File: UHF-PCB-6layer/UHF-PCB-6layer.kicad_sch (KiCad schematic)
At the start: 1 part, among them U1 XC7A100T-CSG324

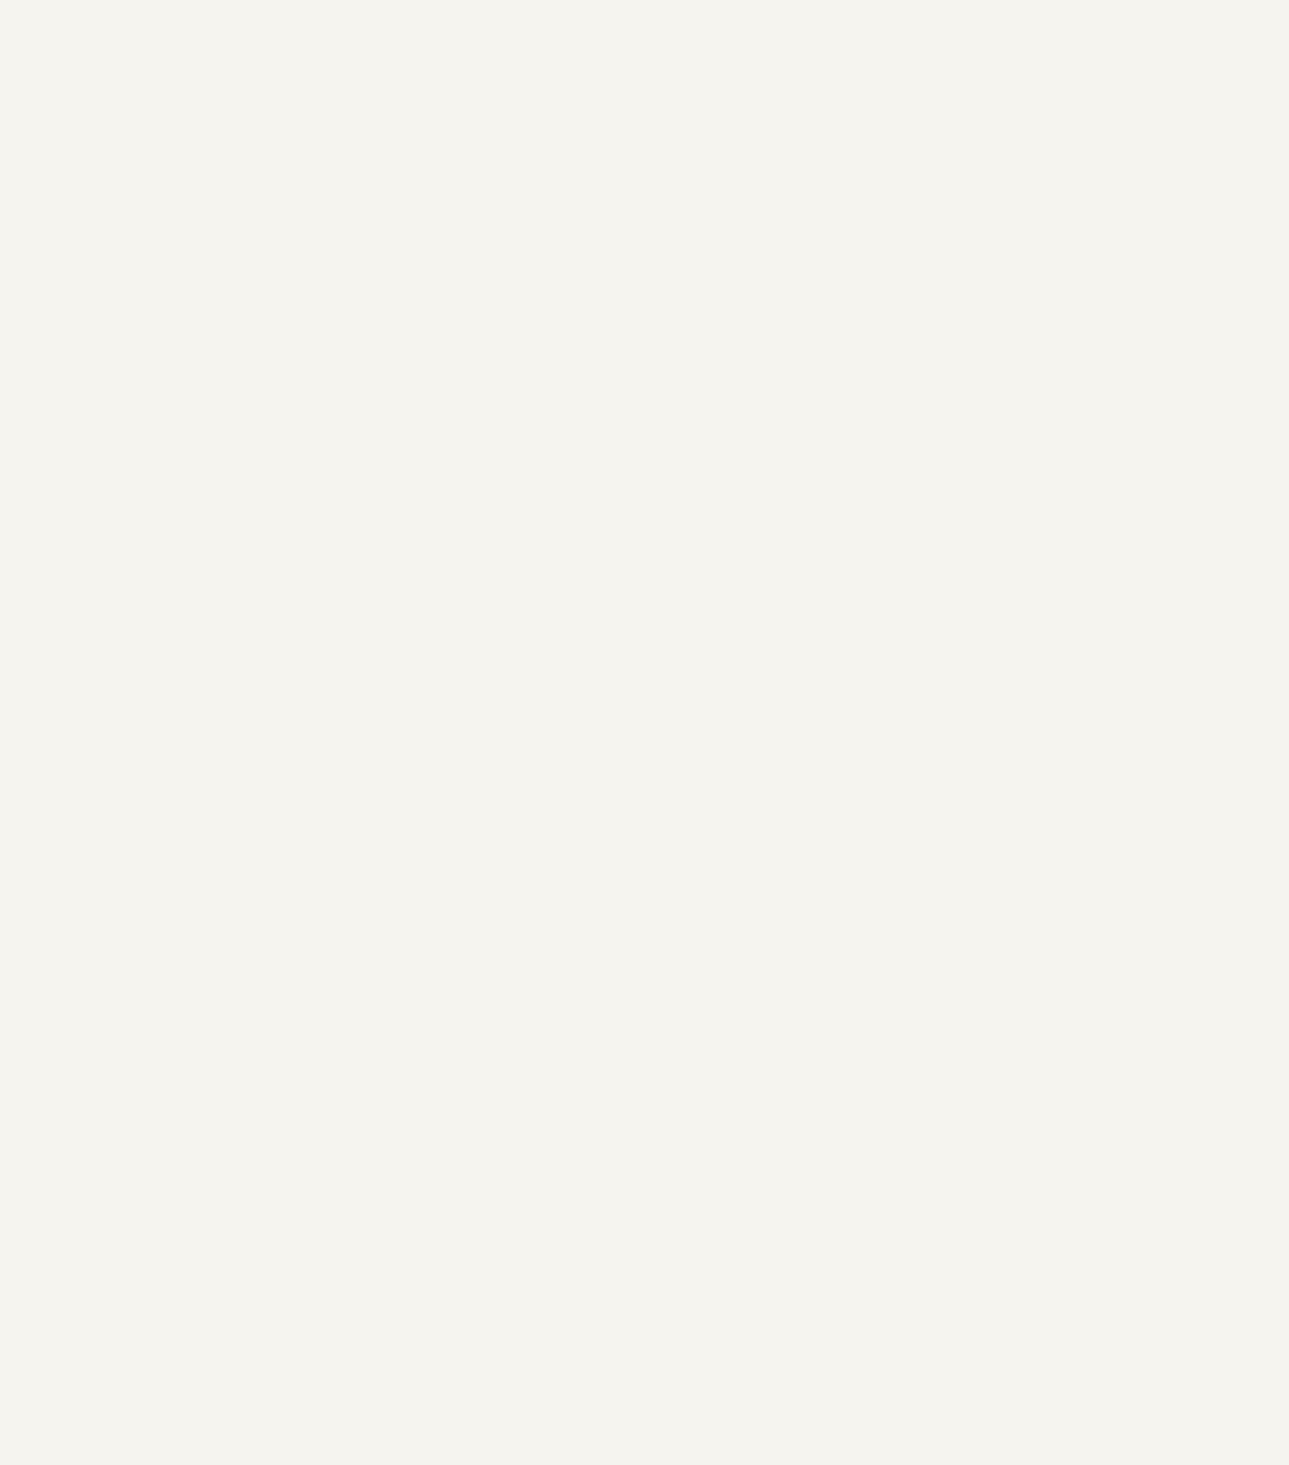
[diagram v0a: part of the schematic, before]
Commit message: added to pcb design, added all comps but mixer and microcontroller
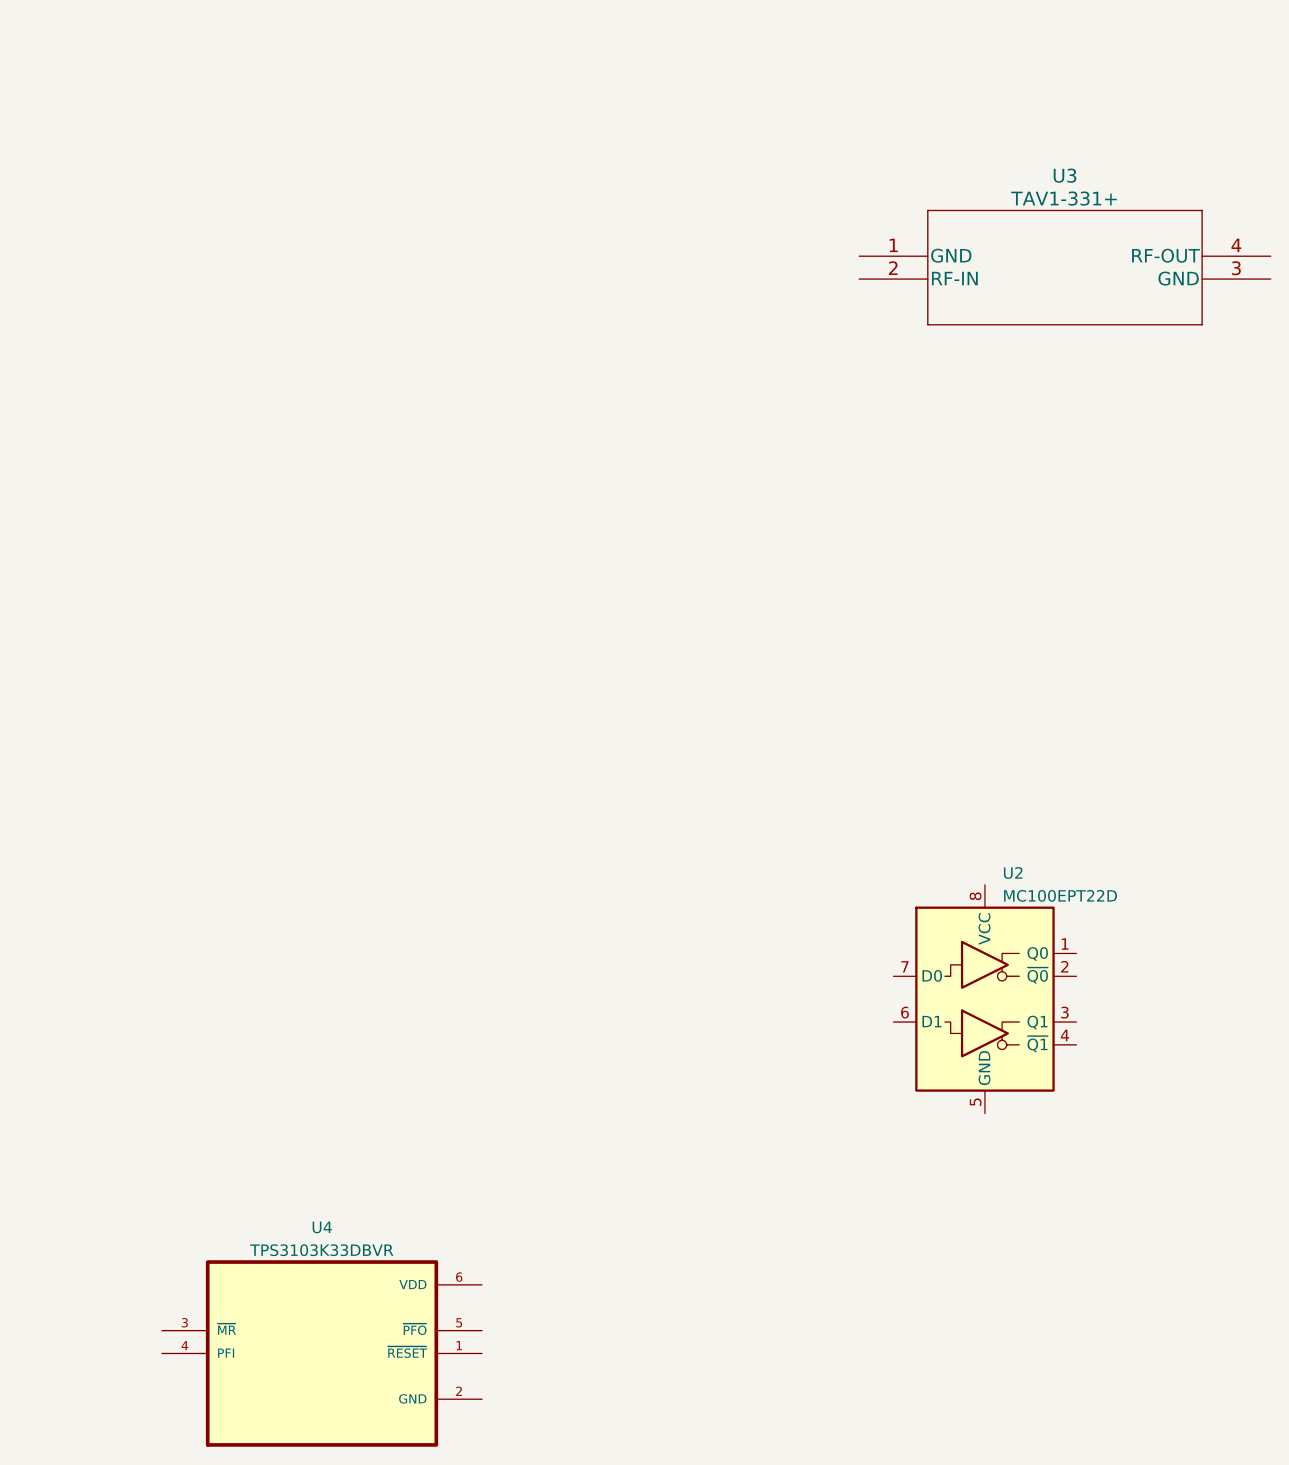
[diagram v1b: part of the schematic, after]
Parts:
- added U2: MC100EPT22D, Package_SO:SOIC-8_3.9x4.9mm_P1.27mm, symbol Interface:MC100EPT22D
- added U3: TAV1-331+, TE2769_MNC, symbol 2023-12-16_21-42-08:TAV1-331+
- added U4: TPS3103K33DBVR, SOT95P280X145-6N, symbol TPS3103K33DBVR:TPS3103K33DBVR
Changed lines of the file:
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@@
+    )
+  )
+  (symbol (lib_id "2023-12-16_21-42-08:TAV1-331+") (at 378.46 52.07 0) (unit 1)
+    (in_bom yes) (on_board yes) (dnp no) (fields_autoplaced)
+    (property "Reference" "U3" (at 401.32 43.18 0)
+      (effects (font (size 1.524 1.524)))
+    )
+    (property "Value" "TAV1-331+" (at 401.32 45.72 0)
+      (effects (font (size 1.524 1.524)))
+    )
+    (property "Footprint" "TE2769_MNC" (at 401.32 45.974 0)
+      (effects (font (size 1.524 1.524)) hide)
+    )
+    (property "Datasheet" "" (at 378.46 52.07 0)
+      (effects (font (size 1.524 1.524)))
+    )
+    (pin "1")
+    (pin "2")
+    (pin "3")
+    (pin "4")
+    (instances
+      (project "UHF-PCB-6layer"
+        (path "/408f5dbf-8c57-4b84-b0cc-1d788fcf6d08"
+          (reference "U3") (unit 1)
+        )
+      )
+    )
+  )
+  (symbol (lib_id "Interface:MC100EPT22D") (at 392.43 134.62 0) (unit 1)
+    (in_bom yes) (on_board yes) (dnp no) (fields_autoplaced)
+    (property "Reference" "U2" (at 394.3859 120.65 0)
+      (effects (font (size 1.27 1.27)) (justify left))
+    )
+    (property "Value" "MC100EPT22D" (at 394.3859 123.19 0)
+      (effects (font (size 1.27 1.27)) (justify left))
+    )
+    (property "Footprint" "Package_SO:SOIC-8_3.9x4.9mm_P1.27mm" (at 389.89 158.75 0)
+      (effects (font (size 1.27 1.27)) hide)
+    )
+    (property "Datasheet" "https://www.onsemi.com/pub/Collateral/MC100EPT22-D.PDF" (at 393.7 144.78 0)
+      (effects (font (size 1.27 1.27)) hide)
+    )
+    (pin "1")
+    (pin "2")
+    (pin "3")
+    (pin "4")
+    (pin "5")
+    (pin "6")
+    (pin "7")
+    (pin "8")
+    (instances
+      (project "UHF-PCB-6layer"
+        (path "/408f5dbf-8c57-4b84-b0cc-1d788fcf6d08"
+          (reference "U2") (unit 1)
+        )
+      )
+    )
+  )
+  (symbol (lib_id "TPS3103K33DBVR:TPS3103K33DBVR") (at 318.77 173.99 0) (unit 1)
+    (in_bom yes) (on_board yes) (dnp no) (fields_autoplaced)
+    (property "Reference" "U4" (at 318.77 160.02 0)
+      (effects (font (size 1.27 1.27)))
+    )
+    (property "Value" "TPS3103K33DBVR" (at 318.77 162.56 0)
+      (effects (font (size 1.27 1.27)))
+    )
+    (property "Footprint" "SOT95P280X145-6N" (at 318.77 173.99 0)
+      (effects (font (size 1.27 1.27)) (justify left bottom) hide)
+    )
+    (property "Datasheet" "" (at 318.77 173.99 0)
+      (effects (font (size 1.27 1.27)) (justify left bottom) hide)
+    )
+    (pin "1")
+    (pin "2")
+    (pin "3")
+    (pin "4")
+    (pin "5")
+    (pin "6")
+    (instances
+      (project "UHF-PCB-6layer"
+        (path "/408f5dbf-8c57-4b84-b0cc-1d788fcf6d08"
+          (reference "U4") (unit 1)
+        )
+      )
     )
   )

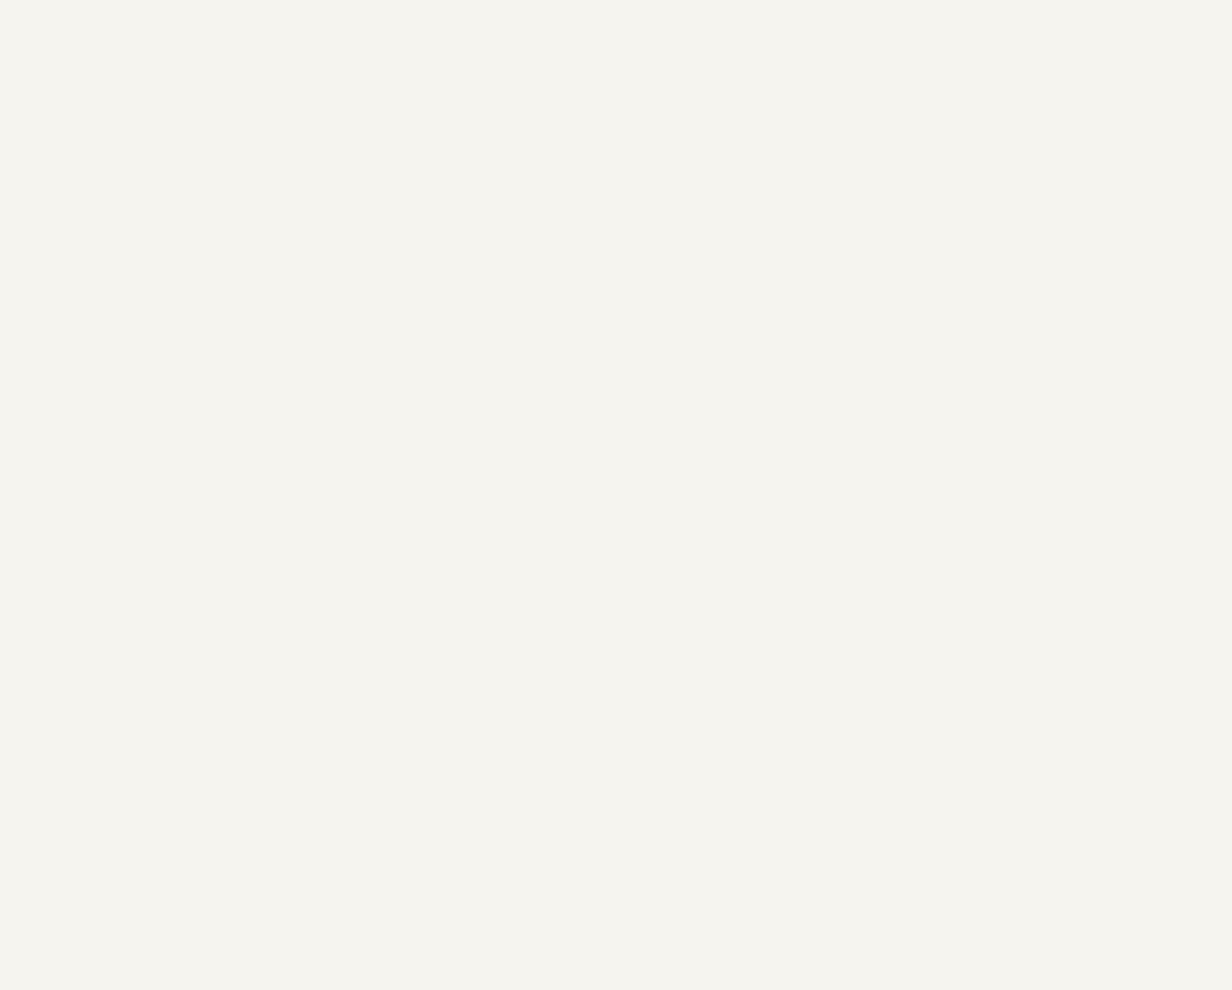
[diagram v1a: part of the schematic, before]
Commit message: added microcontroller to schematic
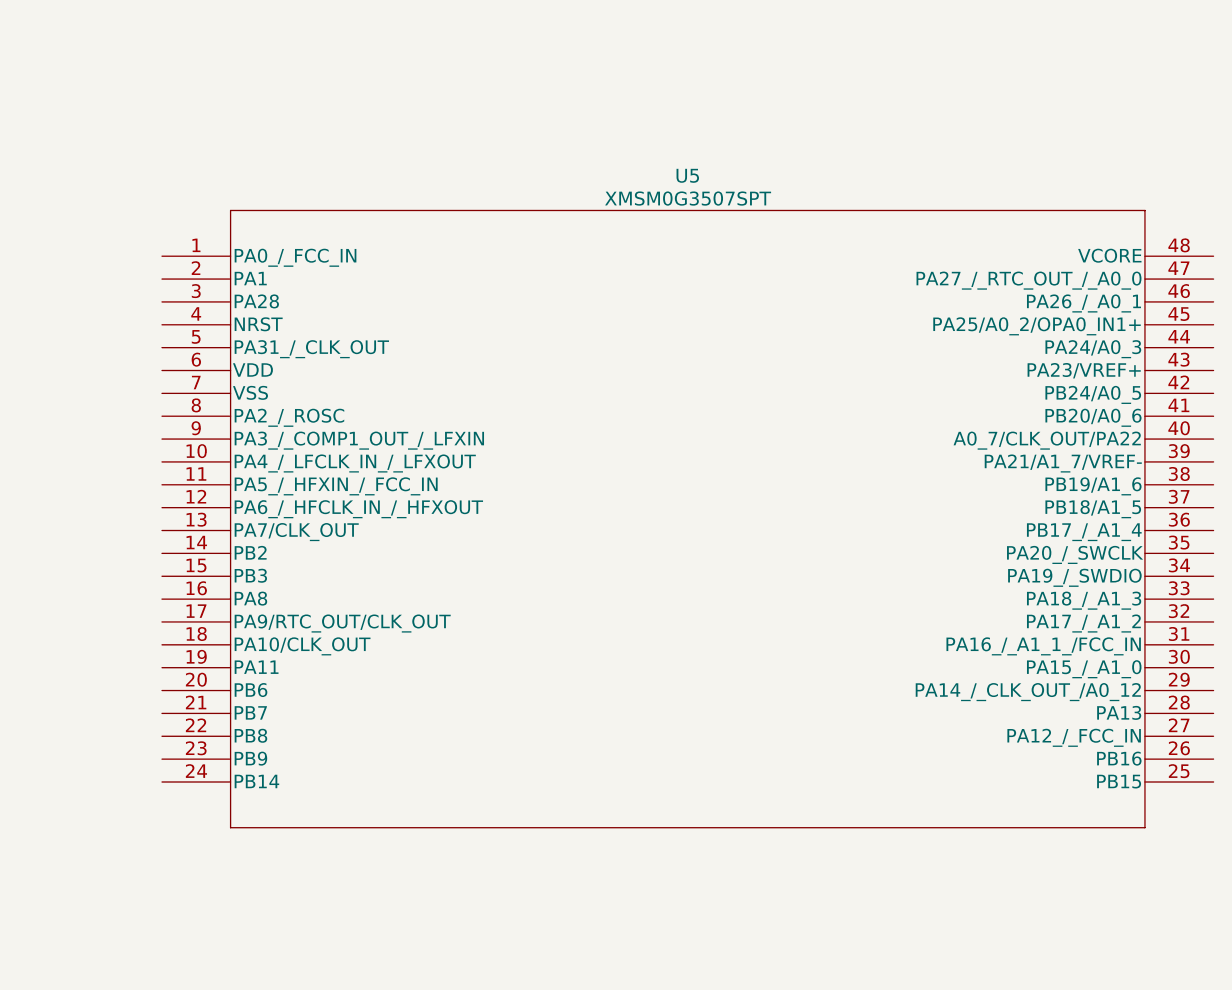
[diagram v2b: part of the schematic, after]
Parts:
- added U5: XMSM0G3507SPT, LQFP48_PT_TEX, symbol 2023-12-17_23-20-25:XMSM0G3507SPT
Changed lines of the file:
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@@
+    )
+  )
+  (symbol (lib_id "2023-12-17_23-20-25:XMSM0G3507SPT") (at 542.29 102.87 0) (unit 1)
+    (in_bom yes) (on_board yes) (dnp no) (fields_autoplaced)
+    (property "Reference" "U5" (at 600.71 93.98 0)
+      (effects (font (size 1.524 1.524)))
+    )
+    (property "Value" "XMSM0G3507SPT" (at 600.71 96.52 0)
+      (effects (font (size 1.524 1.524)))
+    )
+    (property "Footprint" "LQFP48_PT_TEX" (at 600.71 96.774 0)
+      (effects (font (size 1.524 1.524)) hide)
+    )
+    (property "Datasheet" "" (at 542.29 102.87 0)
+      (effects (font (size 1.524 1.524)))
+    )
+    (pin "1")
+    (pin "10")
+    (pin "11")
+    (pin "12")
+    (pin "13")
+    (pin "14")
+    (pin "15")
+    (pin "16")
+    (pin "17")
+    (pin "18")
+    (pin "19")
+    (pin "2")
+    (pin "20")
+    (pin "21")
+    (pin "22")
+    (pin "23")
+    (pin "24")
+    (pin "25")
+    (pin "26")
+    (pin "27")
+    (pin "28")
+    (pin "29")
+    (pin "3")
+    (pin "30")
+    (pin "31")
+    (pin "32")
+    (pin "33")
+    (pin "34")
+    (pin "35")
+    (pin "36")
+    (pin "37")
+    (pin "38")
+    (pin "39")
+    (pin "4")
+    (pin "40")
+    (pin "41")
+    (pin "42")
+    (pin "43")
+    (pin "44")
+    (pin "45")
+    (pin "46")
+    (pin "47")
+    (pin "48")
+    (pin "5")
+    (pin "6")
+    (pin "7")
+    (pin "8")
+    (pin "9")
+    (instances
+      (project "UHF-PCB-6layer"
+        (path "/408f5dbf-8c57-4b84-b0cc-1d788fcf6d08"
+          (reference "U5") (unit 1)
+        )
+      )
     )
   )
